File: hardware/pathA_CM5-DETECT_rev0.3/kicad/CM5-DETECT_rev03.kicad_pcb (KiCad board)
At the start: 4 copper layers, 44 x 134 mm, 192 parts, among them M1 Raspberry Pi CM5 (CM5108032 /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

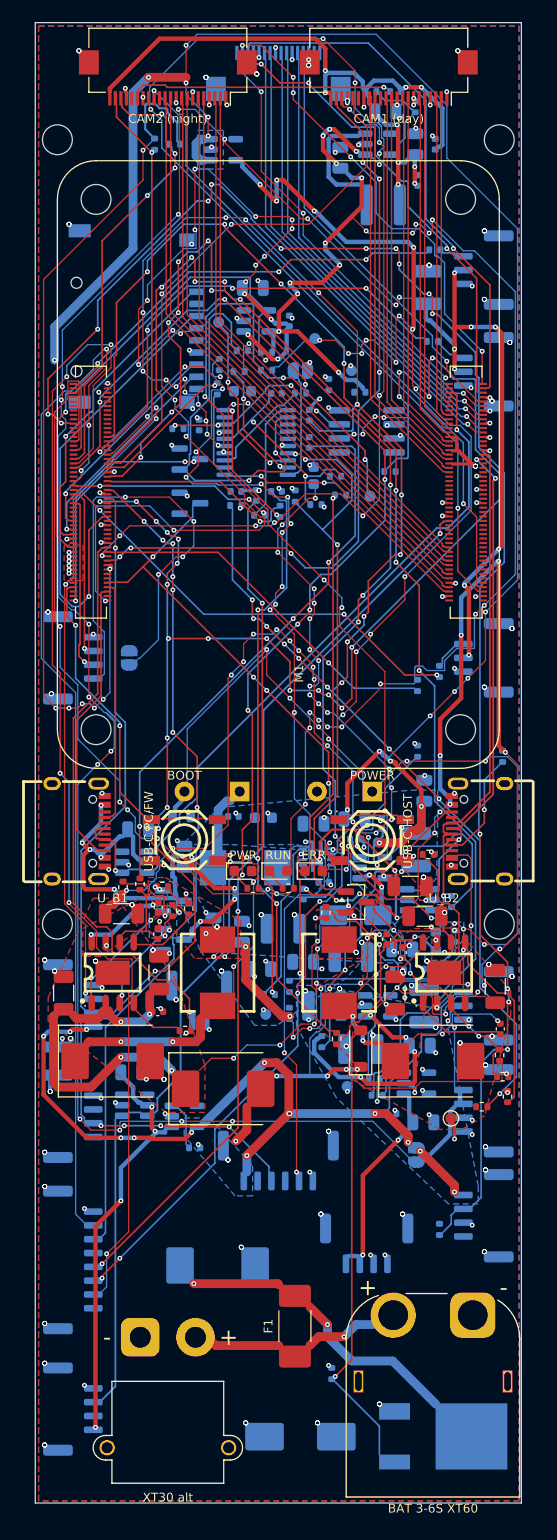
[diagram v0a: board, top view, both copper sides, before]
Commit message: rev0.3: fix routed board project file (netclasses), DSN keepouts for edge and CM5 holes
Co-Authored-By: Claude Opus 5.5 <noreply@anthropic.com>
Claude-Session: https://claude.ai/code/session_01QU2atnSo3eyX8zZazu88cn
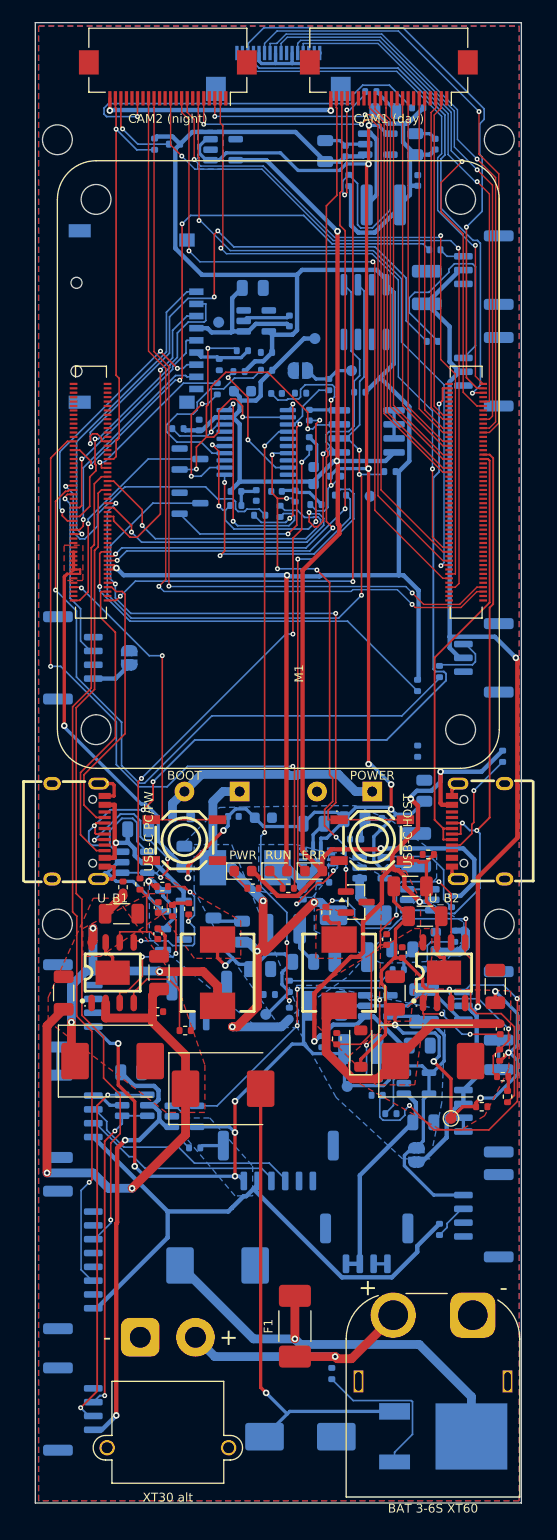
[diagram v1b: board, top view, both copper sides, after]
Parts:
- added C55: 47uF 16V, C_1210_3225Metric, B.Cu at (35.4, 24.0)
- added U_SEC: ATECC608B secure element (I2C 0x60), SOIC-8_3.9x4.9mm_P1.27mm, B.Cu at (29.8, 26.2)
- C54: value 47uF 16V -> 100nF; footprint C_1210_3225Metric -> C_0402_1005Metric
- moved C54 14.4 mm to (28.1, 11.6)
- moved R26 8.29 mm to (28.4, 14.3), turned to 90 degrees
- moved R27 4.25 mm to (30.4, 6.24), turned to 0 degrees
- moved R33 2.48 mm to (34.6, 7.72)
- moved C7 1.50 mm to (26.2, 11.6)
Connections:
- C54 pad 1: VSERVO -> +3V3_CM5
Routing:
- net FAN_PWM: track 146.9 -> 3.36 mm, vias 15 -> 0
- net IO_GPIO11: track 134.1 -> 0.00 mm, vias 11 -> 0
- net VBAT_SENSE: track 157.2 -> 28.3 mm, vias 28 -> 4
- net VSERVO: track 225.0 -> 97.4 mm, vias 26 -> 2
- net SERVO4_G: track 118.9 -> 0.00 mm, vias 7 -> 0
- net IO_GPIO7: track 106.6 -> 0.00 mm, vias 5 -> 0
- net TH_SYNC: track 103.1 -> 0.00 mm, vias 15 -> 0
- net GND: track 33.5 -> 130.8 mm, vias 306 -> 0
- net IO_GPIO24: track 96.7 -> 0.00 mm, vias 3 -> 0
- net I2C1_SCL: track 172.9 -> 85.7 mm, vias 31 -> 4
- net USB1_DN: track 0.00 -> 81.8 mm, vias 0 -> 4
- net I2C1_SDA: track 0.00 -> 72.9 mm, vias 0 -> 3
- net VBUS2: track 126.7 -> 57.4 mm, vias 18 -> 4
- net UART2_RX: track 65.7 -> 0.00 mm, vias 5 -> 0
- net IO_GPIO10: track 141.3 -> 76.1 mm, vias 17 -> 1
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
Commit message: rev0.3: render fixes (hybrid module model, zoom), routed board f15
Co-Authored-By: Claude Opus 5.5 <noreply@anthropic.com>
Claude-Session: https://claude.ai/code/session_01QU2atnSo3eyX8zZazu88cn
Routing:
- net IO_GPIO16: track 0.00 -> 119.3 mm, vias 0 -> 3
- net FAN_PWM: track 3.36 -> 117.7 mm, vias 0 -> 5
- net FAN_TACH: track 0.00 -> 108.9 mm, vias 0 -> 3
- net IO_GPIO7: track 0.00 -> 81.1 mm, vias 0 -> 3
- net SERVO4_G: track 0.00 -> 80.1 mm, vias 0 -> 3
- net CAM1_GPIO0: track 0.00 -> 79.7 mm, vias 0 -> 2
- net TH_SYNC: track 0.00 -> 78.1 mm, vias 0 -> 1
- net IO_GPIO24: track 0.00 -> 78.0 mm, vias 0 -> 3
- net CAM2_D3_P: track 76.0 -> 0.00 mm, vias 2 -> 0
- net USB1_DP: track 16.8 -> 86.9 mm, vias 3 -> 4
- net CAM2_D2_P: track 0.00 -> 68.3 mm, vias 0 -> 4
- net I2C1_SDA: track 72.9 -> 138.9 mm, vias 3 -> 6
- net GND: track 130.8 -> 196.4 mm
- net UART2_RX: track 0.00 -> 56.6 mm, vias 0 -> 1
- net SERVO2_G: track 53.5 -> 0.00 mm, vias 3 -> 0
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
